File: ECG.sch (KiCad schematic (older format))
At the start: 41 parts, among them J1 SJ-3566AN, J2 Conn_01x02_Male, Q1 MMBT3904-7-F, U1 ADR4525, U2 SP6641, U7 ADS1015IDGS

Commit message: Added GND to I2C header and added ground and power planes.
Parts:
- removed J2: Conn_01x02_Male, Connector_PinHeader_2.00mm:PinHeader_1x02_P2.00mm_Vertical, symbol Connector:Conn_01x02_Male
- added J2: Conn_01x03, Connector_PinHeader_1.00mm:PinHeader_1x03_P1.00mm_Vertical, symbol Connector_Generic:Conn_01x03
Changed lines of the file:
@@
 	1    0    0    -1
 $EndComp
-Text GLabel 2100 6500 0    50   Input ~ 0
-SHDN
 $Comp
 L Device:LED D2
@@
 	1    10325 2800
 	1    0    0    -1
-$EndComp
-$Comp
-L Connector:Conn_01x02_Male J2
-U 1 1 5FBFCC75
-P 10975 3700
-F 0 "J2" H 10947 3582 50  0000 R CNN
-F 1 "Conn_01x02_Male" H 11525 3775 50  0000 R CNN
-F 2 "Connector_PinHeader_2.00mm:PinHeader_1x02_P2.00mm_Vertical" H 10975 3700 50  0001 C CNN
-F 3 "~" H 10975 3700 50  0001 C CNN
-	1    10975 3700
-	-1   0    0    1
 $EndComp
 $Comp
@@
 Wire Wire Line
 	10575 3600 10775 3600
-Connection ~ 10775 3600
 Wire Wire Line
 	10775 3275 10775 3600
@@
 Text GLabel 9025 3800 0    50   Input ~ 0
 2.5V
+Text GLabel 2100 6500 0    50   Input ~ 0
+5V
+$Comp
+L Connector_Generic:Conn_01x03 J2
+U 1 1 5FCF854F
+P 10975 3700
+F 0 "J2" H 11055 3742 50  0000 L CNN
+F 1 "Conn_01x03" H 11055 3651 50  0000 L CNN
+F 2 "Connector_PinHeader_1.00mm:PinHeader_1x03_P1.00mm_Vertical" H 10975 3700 50  0001 C CNN
+F 3 "~" H 10975 3700 50  0001 C CNN
+	1    10975 3700
+	1    0    0    -1
+$EndComp
+Connection ~ 10775 3600
+$Comp
+L power:GND #PWR020
+U 1 1 5FCF90A6
+P 10775 3800
+F 0 "#PWR020" H 10775 3550 50  0001 C CNN
+F 1 "GND" H 10780 3627 50  0000 C CNN
+F 2 "" H 10775 3800 50  0001 C CNN
+F 3 "" H 10775 3800 50  0001 C CNN
+	1    10775 3800
+	1    0    0    -1
+$EndComp
 $EndSCHEMATC

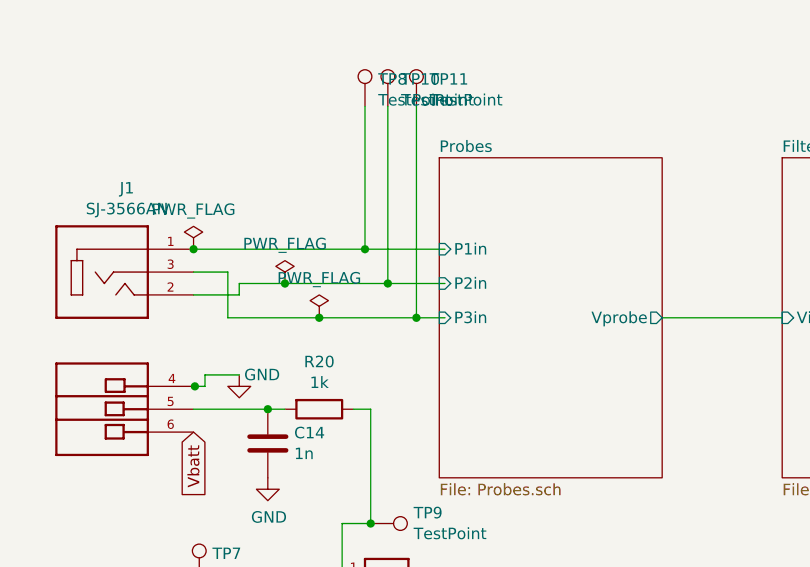
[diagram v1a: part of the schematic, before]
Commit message: #4 - Initial component placement complete. Increased board size.
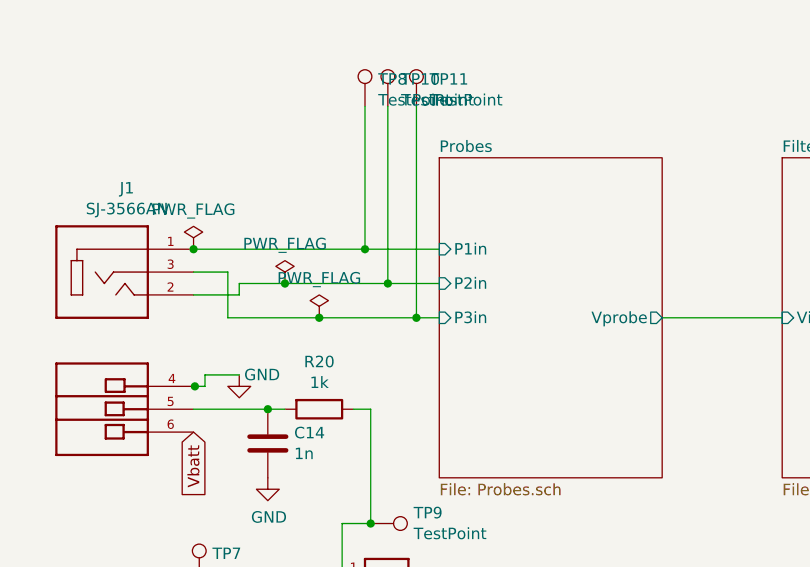
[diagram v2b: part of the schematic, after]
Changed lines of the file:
@@
 F1 "Probes.sch" 50
 F2 "Vprobe" O R 7050 3500 50
-F3 "P1in" I L 6075 3200 50
-F4 "P2in" I L 6075 3350 50
-F5 "P3in" I L 6075 3500 50
+F3 "P2in" I L 6075 3350 50
+F4 "P3in" I L 6075 3500 50
+F5 "P1in" I L 6075 3200 50
 $EndSheet
 $Sheet
@@
 Wire Wire Line
 	5750 2575 5750 3200
-Connection ~ 5750 3200
-Wire Wire Line
-	5750 3200 6100 3200
-Wire Wire Line
-	5850 2575 5850 3350
-Connection ~ 5850 3350
-Wire Wire Line
-	5850 3350 6100 3350
 Wire Wire Line
 	5975 2575 5975 3500
-Connection ~ 5975 3500
-Wire Wire Line
-	5975 3500 6100 3500
 $Comp
 L Connector:TestPoint TP9
@@
 	1    0    0    -1
 $EndComp
+Wire Wire Line
+	6075 3200 5750 3200
+Connection ~ 5750 3200
+Wire Wire Line
+	5850 2575 5850 3350
+Wire Wire Line
+	6075 3350 5850 3350
+Connection ~ 5850 3350
+Wire Wire Line
+	6075 3500 5975 3500
+Connection ~ 5975 3500
 $EndSCHEMATC

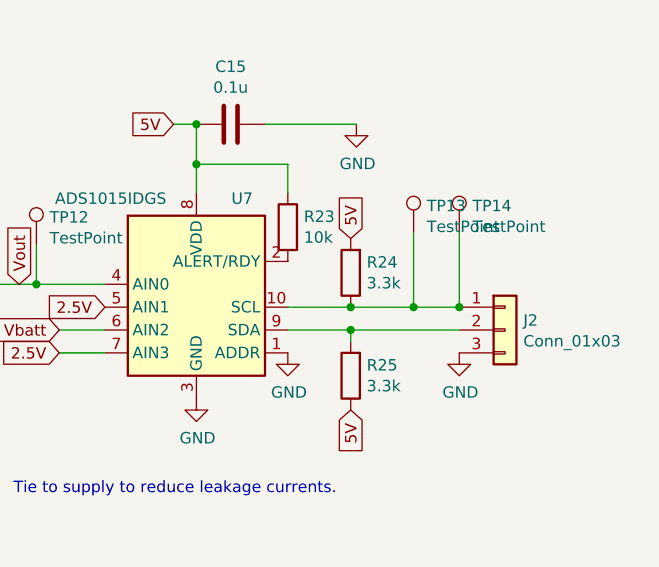
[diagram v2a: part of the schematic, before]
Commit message: #4 - Cleaned up ERC errors and updated the I2C pinout to increase board NET clearance
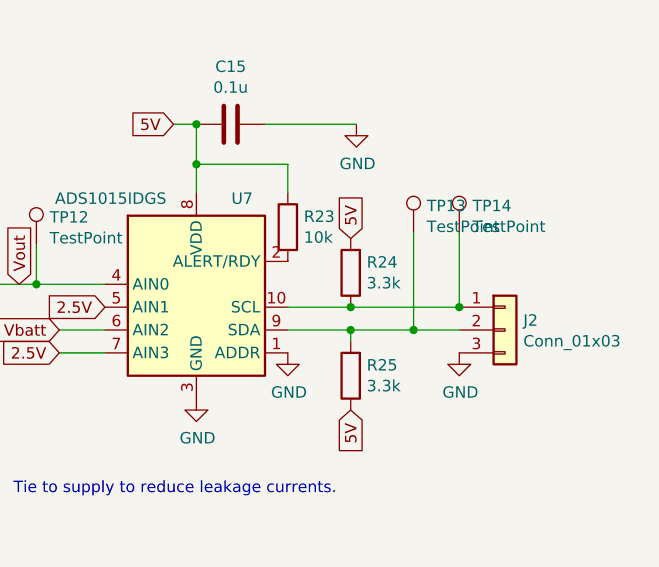
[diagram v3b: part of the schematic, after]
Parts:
- J2: footprint Connector_PinHeader_1.00mm:PinHeader_1x03_P1.00mm_Vertical -> Connector_PinHeader_2.00mm:PinHeader_1x03_P2.00mm_Vertical
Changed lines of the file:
@@
 	10300 3700 10300 3750
 Wire Wire Line
-	10300 3700 10775 3700
+	10300 3700 10575 3700
 Connection ~ 10300 3700
-Wire Wire Line
-	10300 3600 10575 3600
 Wire Wire Line
 	10300 3600 10025 3600
@@
 $EndComp
 Wire Wire Line
-	10575 3275 10575 3600
-Connection ~ 10575 3600
-Wire Wire Line
-	10575 3600 10775 3600
-Wire Wire Line
 	10775 3275 10775 3600
 $Comp
@@
 F 0 "J2" H 11055 3742 50  0000 L CNN
 F 1 "Conn_01x03" H 11055 3651 50  0000 L CNN
-F 2 "Connector_PinHeader_1.00mm:PinHeader_1x03_P1.00mm_Vertical" H 10975 3700 50  0001 C CNN
+F 2 "Connector_PinHeader_2.00mm:PinHeader_1x03_P2.00mm_Vertical" H 10975 3700 50  0001 C CNN
 F 3 "~" H 10975 3700 50  0001 C CNN
 	1    10975 3700
@@
 	6075 3500 5975 3500
 Connection ~ 5975 3500
+Connection ~ 10575 3700
+Wire Wire Line
+	10575 3700 10775 3700
+Wire Wire Line
+	10300 3600 10775 3600
+Wire Wire Line
+	10575 3275 10575 3700
 $EndSCHEMATC

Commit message: #5 - Added 3.3V buck-boost regulator
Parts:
- removed C2: 1uF, Capacitor_SMD:C_0805_2012Metric_Pad1.18x1.45mm_HandSolder, symbol Device:CP1
- removed D1: D_Schottky, Diode_SMD:D_SOD-323_HandSoldering, symbol Device:D_Schottky
- removed R19: 10, Resistor_SMD:R_0805_2012Metric_Pad1.20x1.40mm_HandSolder, symbol Device:R
- removed U2: SP6641, Package_TO_SOT_SMD:SOT-23-5, symbol Regulators:SP6641
- added C16: 1uF, symbol Device:C
- added C2: 2.2uF, symbol Device:C
- added U2: LTC3531, Package_TO_SOT_SMD:TSOT-23-6, symbol Regulators:LTC3531
- C3: footprint Capacitor_SMD:CP_Elec_6.3x5.3 -> Capacitor_SMD:CP_Elec_5x5.3
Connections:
- net labels added: 3.3V
- net labels removed: 5V
- wire segments 77 -> 84
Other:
- moved on the sheet: C1, L1, TP1, TP4

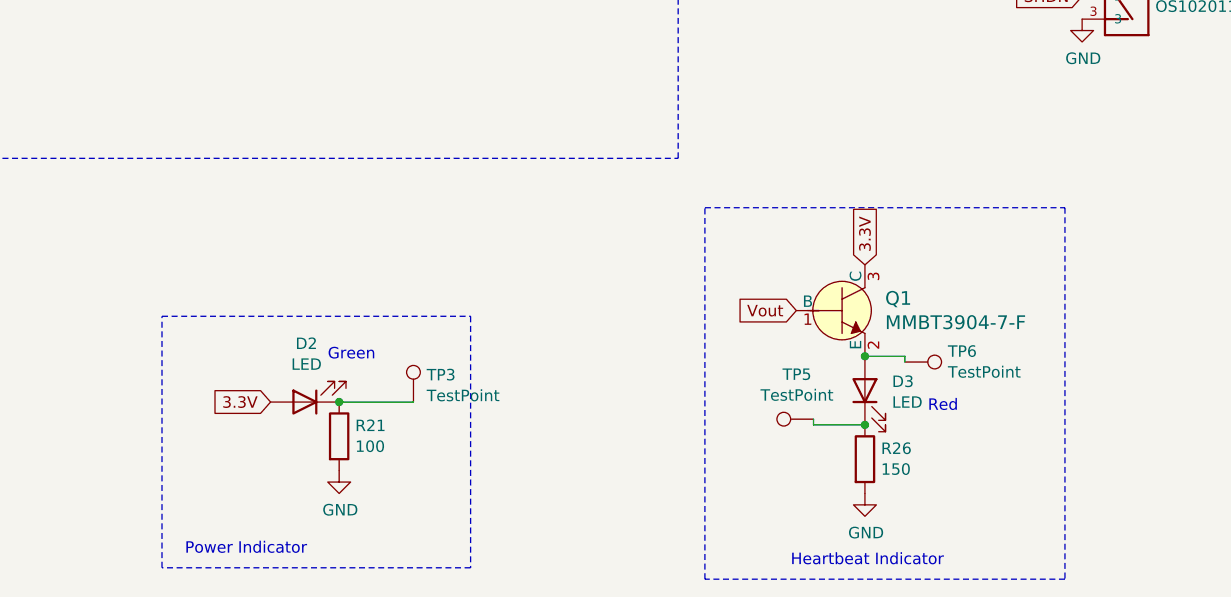
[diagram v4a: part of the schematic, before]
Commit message: #13 and #5 - Updated circuits for 3.3V power rail
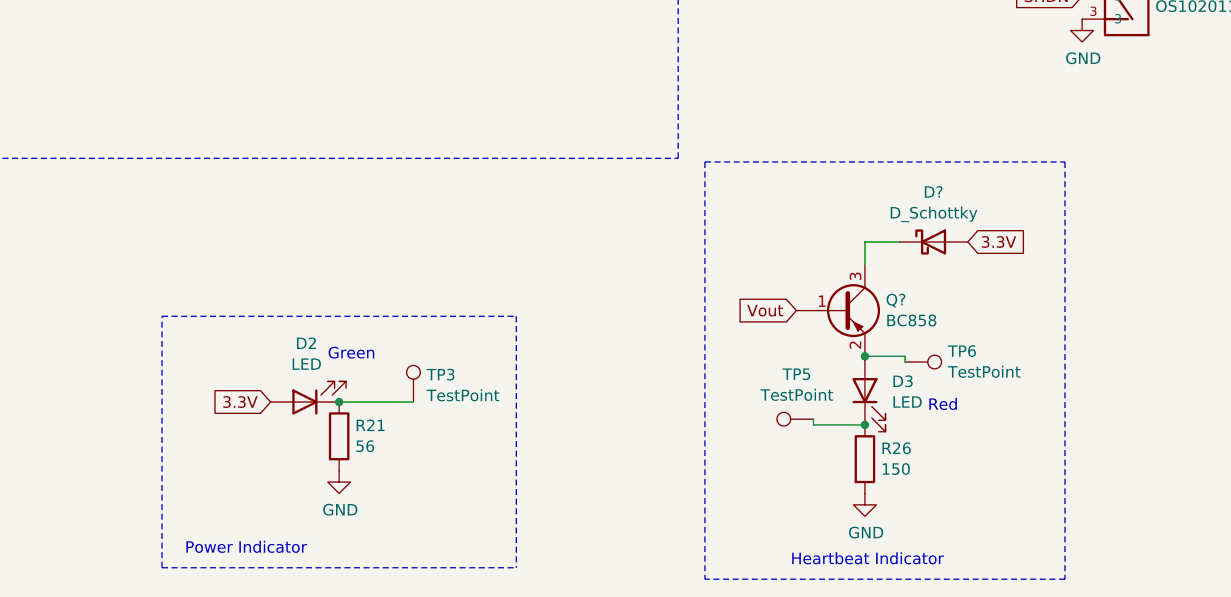
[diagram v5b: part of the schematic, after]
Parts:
- removed Q1: MMBT3904-7-F, digikey-footprints:SOT-23-3, symbol dk_Transistors-Bipolar-BJT-Single:MMBT3904-7-F
- added D?: D_Schottky, Diode_SMD:D_0603_1608Metric_Pad1.05x0.95mm_HandSolder, symbol Device:D_Schottky
- added Q?: BC858, Package_TO_SOT_SMD:SOT-23, symbol Transistor_BJT:BC858
- R21: value 100 -> 56
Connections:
- net 3.3V: now also D?.2 (A)
- net Vout: now also Q?.1 (B)
- net at D3.2 (A), TP6.1: now also Q?.2 (E)
- new net: D?.1 (K), Q?.3 (C)
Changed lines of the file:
@@
 F5 "P1in" I L 6075 3200 50
-$EndSheet
-$Sheet
-S 7575 2800 1075 1400
-U 5F9F8E33
-F0 "Filters_And_Gain" 50
-F1 "Filters_and_Gain.sch" 50
-F2 "Vout" O R 8650 3500 50
-F3 "Vin" I L 7575 3500 50
 $EndSheet
 Text GLabel 2400 3900 2    50   Input Italic 0
@@
 P 2400 6650
 F 0 "R21" H 2470 6696 50  0000 L CNN
-F 1 "100" H 2470 6605 50  0000 L CNN
+F 1 "56" H 2470 6605 50  0000 L CNN
 F 2 "Resistor_SMD:R_0805_2012Metric_Pad1.20x1.40mm_HandSolder" V 2330 6650 50  0001 C CNN
 F 3 "~" H 2400 6650 50  0001 C CNN
@@
 F 1 "LED" H 2243 6336 50  0000 C CNN
 F 2 "Diode_SMD:D_0603_1608Metric_Pad1.05x0.95mm_HandSolder" H 2250 6500 50  0001 C CNN
-F 3 "http://www.qt-brightek.com/datasheet/QBLP601_series.pdf" H 2250 6500 50  0001 C CNN
+F 3 "https://fscdn.rohm.com/en/products/databook/datasheet/opto/led/chip_mono/sml-e1-e.pdf" H 2250 6500 50  0001 C CNN
 	1    2250 6500
 	-1   0    0    1
 $EndComp
 Wire Notes Line
-	2975 6125 2975 7225
-Wire Notes Line
-	2975 7225 1625 7225
+	3175 6125 3175 7225
 Wire Notes Line
 	1625 7225 1625 6125
-Wire Notes Line
-	1625 6125 2975 6125
 Text Notes 1725 7175 0    50   ~ 0
 Power Indicator
@@
 Text Notes 2350 6325 0    50   ~ 0
 Green\n
-$Comp
-L dk_Transistors-Bipolar-BJT-Single:MMBT3904-7-F Q1
-U 1 1 5FC76954
-P 4600 6100
-F 0 "Q1" H 4788 6153 60  0000 L CNN
-F 1 "MMBT3904-7-F" H 4788 6047 60  0000 L CNN
-F 2 "digikey-footprints:SOT-23-3" H 4800 6300 60  0001 L CNN
-F 3 "https://www.diodes.com/assets/Datasheets/ds30036.pdf" H 4800 6400 60  0001 L CNN
-F 4 "MMBT3904-FDICT-ND" H 4800 6500 60  0001 L CNN "Digi-Key_PN"
-F 5 "MMBT3904-7-F" H 4800 6600 60  0001 L CNN "MPN"
-F 6 "Discrete Semiconductor Products" H 4800 6700 60  0001 L CNN "Category"
-F 7 "Transistors - Bipolar (BJT) - Single" H 4800 6800 60  0001 L CNN "Family"
-F 8 "https://www.diodes.com/assets/Datasheets/ds30036.pdf" H 4800 6900 60  0001 L CNN "DK_Datasheet_Link"
-F 9 "/product-detail/en/diodes-incorporated/MMBT3904-7-F/MMBT3904-FDICT-ND/815727" H 4800 7000 60  0001 L CNN "DK_Detail_Page"
-F 10 "TRANS NPN 40V 0.2A SMD SOT23-3" H 4800 7100 60  0001 L CNN "Description"
-F 11 "Diodes Incorporated" H 4800 7200 60  0001 L CNN "Manufacturer"
-F 12 "Active" H 4800 7300 60  0001 L CNN "Status"
-	1    4600 6100
-	1    0    0    -1
-$EndComp
 Text GLabel 8850 3500 1    50   Input ~ 0
 Vout
 Text GLabel 4400 6100 0    50   Input ~ 0
 Vout
-Text GLabel 4700 5900 1    50   Input ~ 0
+Text GLabel 5150 5800 2    50   Input ~ 0
 3.3V
 $Comp
@@
 $EndComp
 Wire Notes Line
-	4000 5650 5575 5650
-Wire Notes Line
-	5575 5650 5575 7275
+	4000 5450 5575 5450
 Wire Notes Line
 	5575 7275 4000 7275
-Wire Notes Line
-	4000 7275 4000 5650
 Text Notes 4375 7225 0    50   ~ 0
 Heartbeat Indicator\n
@@
 Wire Wire Line
 	4875 6300 4875 6325
-Connection ~ 4700 6300
 $Comp
 L Connector:TestPoint TP19
@@
 Text GLabel 1400 2650 0    50   Input ~ 0
 Vbatt
+Wire Notes Line
+	1625 6125 3175 6125
+Wire Notes Line
+	1625 7225 3175 7225
+$Comp
+L Transistor_BJT:BC858 Q?
+U 1 1 5FDAC112
+P 4600 6100
+F 0 "Q?" H 4791 6146 50  0000 L CNN
+F 1 "BC858" H 4791 6055 50  0000 L CNN
+F 2 "Package_TO_SOT_SMD:SOT-23" H 4800 6025 50  0001 L CIN
+F 3 "https://www.onsemi.com/pub/Collateral/BC860-D.pdf" H 4600 6100 50  0001 L CNN
+	1    4600 6100
+	1    0    0    -1
+$EndComp
+Connection ~ 4700 6300
+Wire Wire Line
+	4700 5800 4700 5900
+Wire Notes Line
+	4000 5450 4000 7275
+Wire Notes Line
+	5575 5450 5575 7275
+$Comp
+L Device:D_Schottky D?
+U 1 1 5FDC078D
+P 5000 5800
+F 0 "D?" H 5000 6017 50  0000 C CNN
+F 1 "D_Schottky" H 5000 5926 50  0000 C CNN
+F 2 "Diode_SMD:D_0603_1608Metric_Pad1.05x0.95mm_HandSolder" H 5000 5800 50  0001 C CNN
+F 3 "~" H 5000 5800 50  0001 C CNN
+	1    5000 5800
+	1    0    0    -1
+$EndComp
+Wire Wire Line
+	4700 5800 4850 5800
+$Sheet
+S 7575 2800 1075 1400
+U 5F9F8E33
+F0 "Filters_And_Gain" 50
+F1 "Filters_and_Gain.sch" 50
+F2 "Vout" O R 8650 3500 50
+F3 "Vin" I L 7575 3500 50
+$EndSheet
 $EndSCHEMATC
